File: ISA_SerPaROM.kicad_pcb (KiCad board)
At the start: 2 copper layers, 176.5 x 90.2 mm, 70 parts, among them J1 ISA BUS, J10 Parallel Port, J2 ADDR_IRQ, J3 UART1_SEL, J4 UART2_SEL, J5 Parallel Port LEDs, J6 Serial 2 IDC, J7 Serial 1 DB9, J9 Parport IRQ Select, U1 74LS138, U11 74LS30, U12 74LS86, U13 74LS02, U14 74LS155, U15 74LS245, U16 74LS174, U17 74LS374, U18 74LS05, U19 74LS125, U2 74LS138, U20 74LS240, U21 74LS244, U22 16550, U4 16550, U5 GD75232N, U6 GD75232N, X1 1.8432Mhz

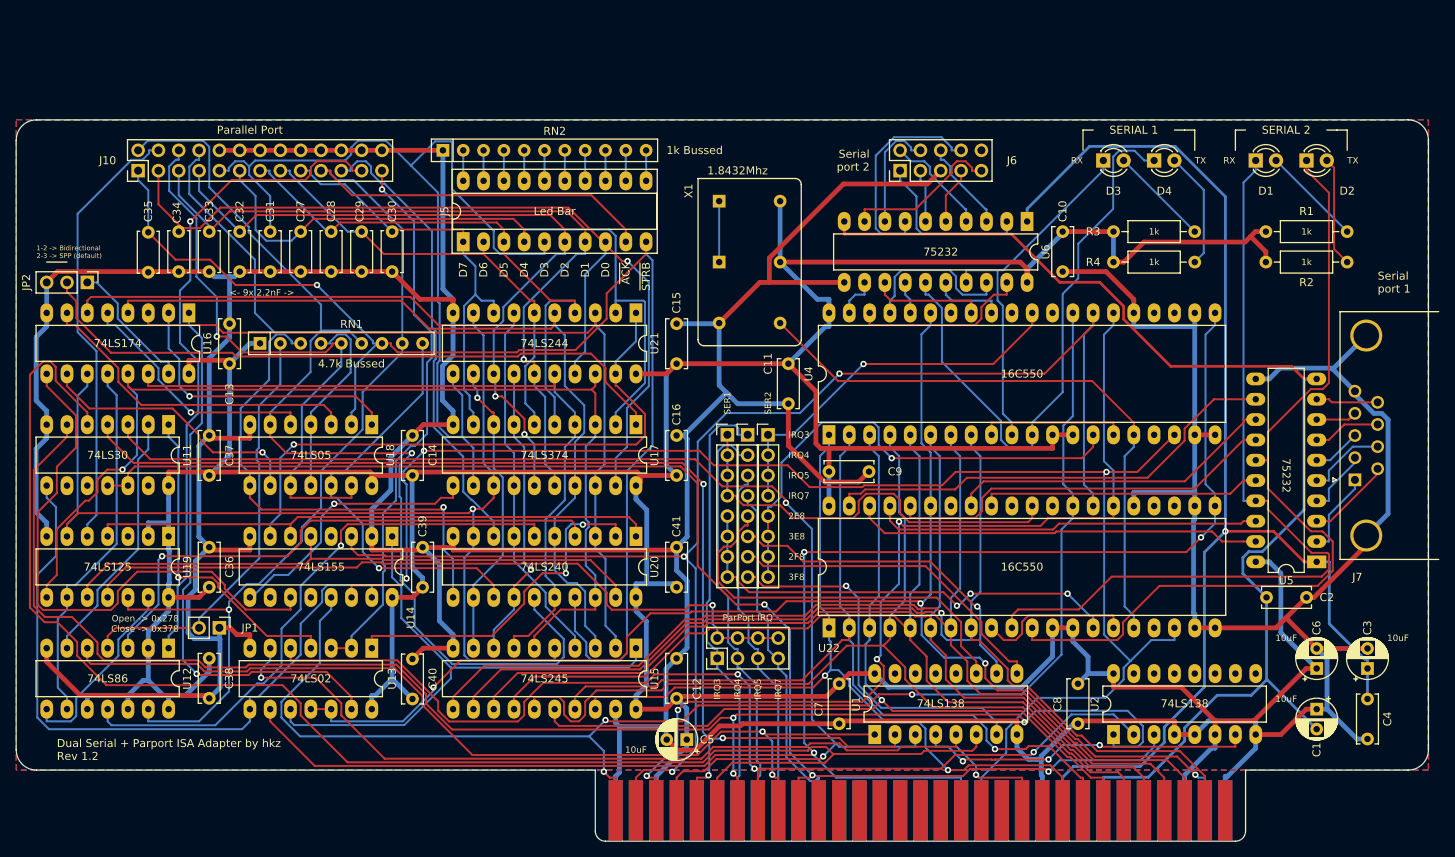
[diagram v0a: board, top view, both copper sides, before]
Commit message: Route Serial/Parallel/ROM board
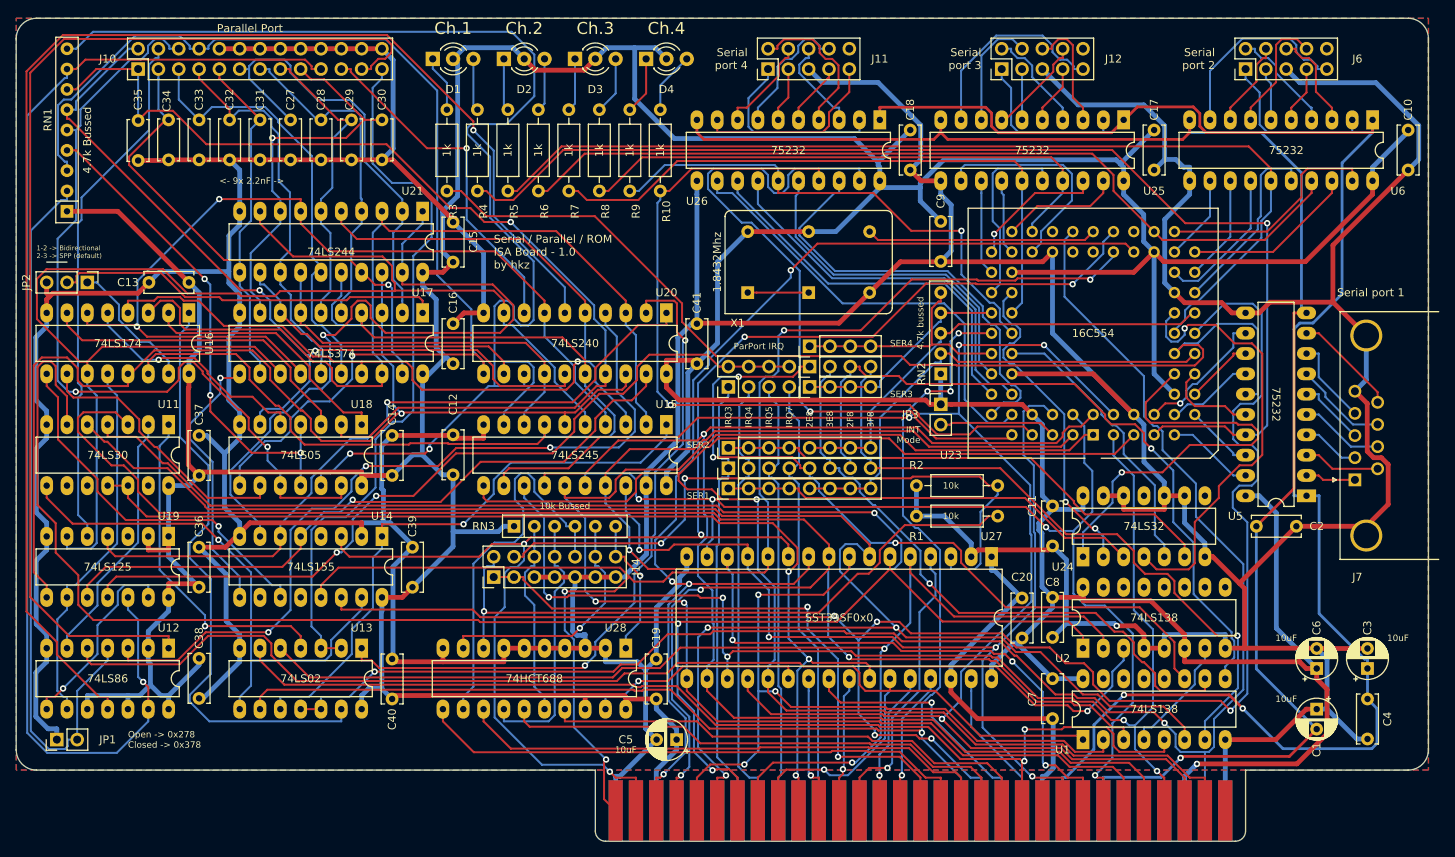
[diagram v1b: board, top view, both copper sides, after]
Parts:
- removed U22, U4: 16550, Package_DIP:DIP-40_W15.24mm_LongPads
- added C17: 100nF, Capacitor_THT:C_Disc_D6.0mm_W2.5mm_P5.00mm, F.Cu at (280.7, 114.3)
- added C18: 100nF, Capacitor_THT:C_Disc_D6.0mm_W2.5mm_P5.00mm, F.Cu at (250.2, 114.3)
- added C19: 100nF, Capacitor_THT:C_Disc_D6.0mm_W2.5mm_P5.00mm, F.Cu at (218.4, 185.4)
- added C20: 100nF, Capacitor_THT:C_Disc_D6.0mm_W2.5mm_P5.00mm, F.Cu at (264.2, 177.8)
- added J11: Serial 4 IDC, Connector_PinHeader_2.54mm:PinHeader_2x05_P2.54mm_Vertical, F.Cu at (232.4, 106.7)
- added J12: Serial 3 IDC, Connector_PinHeader_2.54mm:PinHeader_2x05_P2.54mm_Vertical, F.Cu at (261.6, 106.7)
- added J13: UART4_SEL, Connector_PinHeader_2.54mm:PinHeader_1x04_P2.54mm_Vertical, F.Cu at (237.6, 141.3)
- added J14: ROM Config, Connector_PinHeader_2.54mm:PinHeader_2x07_P2.54mm_Vertical, F.Cu at (198.1, 170.2)
- added J8: UART3_SEL, Connector_PinHeader_2.54mm:PinHeader_1x04_P2.54mm_Vertical, F.Cu at (237.6, 146.4)
- added JP3: Interrupt Mode, Connector_PinHeader_2.54mm:PinHeader_1x02_P2.54mm_Vertical, F.Cu at (254.0, 148.6)
- added R10: 1k, Resistor_THT:R_Axial_DIN0207_L6.3mm_D2.5mm_P10.16mm_Horizontal, F.Cu at (218.9, 111.8)
- added R5: 1k, Resistor_THT:R_Axial_DIN0207_L6.3mm_D2.5mm_P10.16mm_Horizontal, F.Cu at (199.9, 111.8)
- added R6: 1k, Resistor_THT:R_Axial_DIN0207_L6.3mm_D2.5mm_P10.16mm_Horizontal, F.Cu at (203.7, 111.8)
- added R7: 1k, Resistor_THT:R_Axial_DIN0207_L6.3mm_D2.5mm_P10.16mm_Horizontal, F.Cu at (207.5, 111.8)
- added R8: 1k, Resistor_THT:R_Axial_DIN0207_L6.3mm_D2.5mm_P10.16mm_Horizontal, F.Cu at (211.3, 111.8)
- added R9: 1k, Resistor_THT:R_Axial_DIN0207_L6.3mm_D2.5mm_P10.16mm_Horizontal, F.Cu at (215.1, 111.8)
- added RN3: 10k, Resistor_THT:R_Array_SIP6, F.Cu at (200.7, 163.8)
- added U23: 16C554, Package_LCC:PLCC-68_THT-Socket, F.Cu at (273.1, 152.4)
- added U24: 74LS32, Package_DIP:DIP-14_W7.62mm_LongPads, F.Cu at (271.8, 167.6)
- added U25: GD75232N, Package_DIP:DIP-20_W7.62mm_LongPads, F.Cu at (276.9, 113.0)
- added U26: GD75232N, Package_DIP:DIP-20_W7.62mm_LongPads, F.Cu at (246.4, 113.0)
- added U27: SST39SF040, Package_DIP:DIP-32_W15.24mm_LongPads, F.Cu at (260.4, 167.6)
- added U28: 74HCT688, Package_DIP:DIP-20_W7.62mm_LongPads, F.Cu at (214.6, 179.1)
- D1: value LED RX1 -> LED Channel A; footprint LED_THT:LED_D3.0mm -> LED_THT:LED_D3.0mm-3
- D2: value LED TX1 -> LED Channel B; footprint LED_THT:LED_D3.0mm -> LED_THT:LED_D3.0mm-3
- D3: value LED RX2 -> LED Channel C; footprint LED_THT:LED_D3.0mm -> LED_THT:LED_D3.0mm-3
- D4: value LED TX2 -> LED Channel D; footprint LED_THT:LED_D3.0mm -> LED_THT:LED_D3.0mm-3
- J5: value Parallel Port LEDs -> ADDR; footprint Package_DIP:DIP-20_W7.62mm_Socket_LongPads -> Connector_PinHeader_2.54mm:PinHeader_1x04_P2.54mm_Vertical
- R1, R2: value 1k -> 10k
- RN2: value 1k -> 4.7k; footprint Resistor_THT:R_Array_SIP11 -> Resistor_THT:R_Array_SIP5
- moved D1 103.7 mm to (190.5, 105.4)
- moved D2 101.1 mm to (199.4, 105.4)
- moved R3 94.7 mm to (192.3, 111.8), turned to 270 degrees
- moved R4 91.7 mm to (196.1, 111.8), turned to 270 degrees
- moved RN2 68.2 mm to (254.0, 144.8), turned to 90 degrees
- moved D3 67.3 mm to (208.3, 105.4)
- moved D4 64.8 mm to (217.2, 105.4)
- moved R1 64.5 mm to (251.0, 162.6), turned to 0 degrees
- moved R2 60.7 mm to (251.0, 158.8), turned to 0 degrees
- moved J5 46.0 mm to (237.6, 143.9)
- moved J6 45.0 mm to (292.1, 106.7)
- moved C10 45.0 mm to (312.4, 114.3)
- moved U6 45.0 mm to (308.0, 113.0)
- moved C12 39.5 mm to (193.0, 152.4)
- moved C11 37.5 mm to (268.0, 161.3)
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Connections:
- D1 pad 1: /SIN_1 -> Net-(D1-Pad1)
- D1 pad 2: Net-(D1-Pad2) -> VCC
- D2 pad 1: /SOUT_1 -> Net-(D2-Pad1)
- D2 pad 2: Net-(D2-Pad2) -> VCC
- D3 pad 1: /SIN_2 -> Net-(D3-Pad1)
- D3 pad 2: Net-(D3-Pad2) -> VCC
- D4 pad 1: /SOUT_2 -> Net-(D4-Pad1)
- D4 pad 2: Net-(D4-Pad2) -> VCC
- J1 pad 11: (no net) -> /~MEMW
- J1 pad 12: (no net) -> /~MEMR
- J1 pad 43: (no net) -> /A19
- J1 pad 44: (no net) -> /A18
- J1 pad 45: (no net) -> /A17
- J1 pad 46: (no net) -> /A16
- J1 pad 47: (no net) -> /A15
- J1 pad 48: (no net) -> /A14
- J1 pad 49: (no net) -> /A13
- J1 pad 50: (no net) -> /A12
- J1 pad 51: (no net) -> /A11
- J1 pad 52: (no net) -> /A10
- J5 pad 1: /PARPORT_DATA7 -> /0x2E8
- J5 pad 2: /PARPORT_DATA6 -> /0x3E8
- J5 pad 3: /PARPORT_DATA5 -> /0x2F8
- J5 pad 4: /PARPORT_DATA4 -> /0x3F8
- R1 pad 1: Net-(D1-Pad2) -> GND
- R1 pad 2: VCC -> /COMPARATOR_A15
- R2 pad 1: Net-(D2-Pad2) -> GND
- R2 pad 2: VCC -> /FLASH_A15
- R3 pad 1: Net-(D3-Pad2) -> Net-(D1-Pad1)
- R3 pad 2: VCC -> /TX_A
- R4 pad 1: Net-(D4-Pad2) -> Net-(D1-Pad3)
- R4 pad 2: VCC -> /RX_A
- RN2 pad 1: GND -> VCC
- RN2 pad 2: Net-(J5-Pad20) -> /~UART1_CS
- RN2 pad 3: Net-(J5-Pad19) -> /~UART2_CS
- RN2 pad 4: Net-(J5-Pad18) -> /~UART3_CS
- RN2 pad 5: Net-(J5-Pad17) -> /~UART4_CS
- U5 pad 12: /~RI_1 -> /~RI_A
- U5 pad 13: /~DTR_1 -> /~DTR_A
- U5 pad 14: /~CTS_1 -> /~CTS_A
- U5 pad 15: /SOUT_1 -> /TX_A
- U5 pad 16: /~RTS_1 -> /~RTS_A
- U5 pad 17: /SIN_1 -> /RX_A
- U5 pad 18: /~DSR_1 -> /~DSR_A
- U5 pad 19: /~DCD_1 -> /~DCD_A
- U6 pad 12: /~RI_2 -> /~RI_B
- U6 pad 13: /~DTR_2 -> /~DTR_B
- U6 pad 14: /~CTS_2 -> /~CTS_B
- U6 pad 15: /SOUT_2 -> /TX_B
- U6 pad 16: /~RTS_2 -> /~RTS_B
- U6 pad 17: /SIN_2 -> /RX_B
- U6 pad 18: /~DSR_2 -> /~DSR_B
- U6 pad 19: /~DCD_2 -> /~DCD_B
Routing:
- net GND: track 776.5 -> 995.6 mm, vias 0 -> 1
- net VCC: track 570.3 -> 784.3 mm, vias 0 -> 1
- net /RX_A: track 0.00 -> 146.3 mm, vias 0 -> 1
- net /TX_A: track 0.00 -> 132.4 mm
- net /TX_B: track 0.00 -> 124.7 mm
- net /RX_B: track 0.00 -> 108.2 mm
- net /SOUT_1: track 105.8 -> 0.00 mm
- net /PARPORT_IRQ: track 72.5 -> 175.4 mm
- net /SIN_1: track 102.7 -> 0.00 mm
- net /RN_8: track 53.3 -> 154.0 mm, vias 1 -> 2
- net /RX_D: track 0.00 -> 97.8 mm, vias 0 -> 1
- net /~DCD_D: track 0.00 -> 87.7 mm, vias 0 -> 1
- net /FLASH_A15: track 0.00 -> 84.5 mm, vias 0 -> 2
- net /COMPARATOR_A15: track 0.00 -> 82.6 mm, vias 0 -> 1
- net /TX_C: track 0.00 -> 78.1 mm
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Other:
- board size 176.5 x 90.2 mm -> 176.5 x 102.9 mm
- board text added: "10k"
- board text added: "10k Bussed"
- board text added: "16C554"
- board text added: "4.7k bussed"
- board text added: "74HCT688"
- board text added: "74LS32"
- board text added: "Ch.1"
- board text added: "Ch.2"
- board text added: "Ch.3"
- board text added: "Ch.4"
- board text added: "INT Mode"
- board text added: "Open -> 0x278 Closed -> 0x378"
- board text added: "SER3"
- board text added: "SER4"
- board text added: "SST39SF0x0"
- board text added: "Serial / Parallel / ROM ISA Board - 1.0 by hkz"
- board text added: "Serial port 3"
- board text added: "Serial port 4"
- board text removed: "16C550"
- board text removed: "1k Bussed"
- board text removed: "D0"
- board text removed: "D1"
- board text removed: "D2"
- board text removed: "D3"
- board text removed: "D4"
- board text removed: "D5"
- board text removed: "D6"
- board text removed: "D7"
- board text removed: "Dual Serial + Parport ISA Adapter by hkz Rev 1.2"
- board text removed: "Led Bar"
- board text removed: "Open -> 0x278 Close -> 0x378"
- board text removed: "RX"
- board text removed: "SERIAL 1"
- board text removed: "SERIAL 2"
- board text removed: "TX"
- board text removed: "~ACK"
- board text removed: "~STRB"
